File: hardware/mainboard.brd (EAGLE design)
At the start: 65 x 30 mm, 34 parts, among them IC1 ESP-12E/F, Q1 BC847BS, Q2 BC847BS, Q3 BC847BS

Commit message: Placing elements in layout
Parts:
- moved Q3 61.5 mm to (17.5, 14.5), flipped to the bottom
- moved C2 57.0 mm to (27.0, 2.50), flipped to the bottom
- moved C1 53.4 mm to (27.0, 5.50), flipped to the bottom
- moved R2 50.8 mm to (27.0, 11.5), flipped to the bottom, turned to 180 degrees
- moved R15 50.4 mm to (27.0, 14.5), flipped to the bottom
- moved R14 46.3 mm to (21.0, 5.50), flipped to the bottom
- moved R5 42.9 mm to (27.0, 8.50), flipped to the bottom, turned to 0 degrees
- moved Q2 42.0 mm to (17.5, 18.5), flipped to the bottom, turned to 270 degrees
- moved R22 36.5 mm to (35.5, 24.0), flipped to the bottom, turned to 180 degrees
- moved R10 32.8 mm to (29.5, 24.0), flipped to the bottom, turned to 180 degrees
- moved R13 23.9 mm to (35.5, 27.0), flipped to the bottom, turned to 180 degrees
- moved R9 20.6 mm to (29.5, 27.0), flipped to the bottom
- moved Q1 20.2 mm to (17.5, 22.5), flipped to the bottom, turned to 270 degrees
- moved R11 12.9 mm to (50.0, 26.0), flipped to the bottom, turned to 0 degrees
- moved R12 7.85 mm to (43.5, 26.0), flipped to the bottom, turned to 0 degrees
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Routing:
- net GND: track 9.57 -> 0.00 mm

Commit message: Layout resolved
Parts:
- moved R7 2.50 mm to (6.00, 12.0)
- moved R8 2.50 mm to (6.00, 14.5)
- moved R14 2.12 mm to (22.5, 7.00), turned to 270 degrees
- moved R11 1.41 mm to (49.0, 27.0)
- moved R12 1.12 mm to (43.0, 27.0)
- moved Q1 0.50 mm to (17.5, 22.0)
- moved Q2 0.25 mm to (17.5, 18.2)
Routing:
- net GND: track 0.00 -> 125.1 mm, vias 0 -> 5
- net +3V3: track 0.00 -> 87.8 mm, vias 0 -> 5
- net ESP12_/RESET: track 0.00 -> 59.5 mm, vias 0 -> 1
- net GPIO_RING_HOUSE_DETECT: track 0.00 -> 56.4 mm, vias 0 -> 2
- net ESP12_ENABLE: track 0.00 -> 37.9 mm, vias 0 -> 2
- net N$10: track 0.00 -> 33.4 mm
- net N$11: track 0.00 -> 33.3 mm
- net N$8: track 0.00 -> 25.1 mm, vias 0 -> 1
- net ESP12_/FWUPLOAD: track 4.15 -> 26.2 mm, vias 1 -> 2
- net N$9: track 0.00 -> 22.0 mm, vias 0 -> 2
- net N$3: track 0.00 -> 19.0 mm, vias 0 -> 1
- net GPIO_NO_RESET_ON_RING: track 0.00 -> 16.3 mm, vias 0 -> 1
- net RITTO_RING_HOUSE: track 0.00 -> 15.7 mm
- net N$1: track 0.00 -> 15.3 mm
- net GPIO_10_IN: track 3.70 -> 18.6 mm
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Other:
- outline, holes or cut-outs redrawn

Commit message: Checkpoint commit
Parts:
- turned RESET to 180 degrees
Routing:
- net GND: track 125.1 -> 128.1 mm, vias 5 -> 4
- net +3V3: track 87.8 -> 89.5 mm, vias 5 -> 3

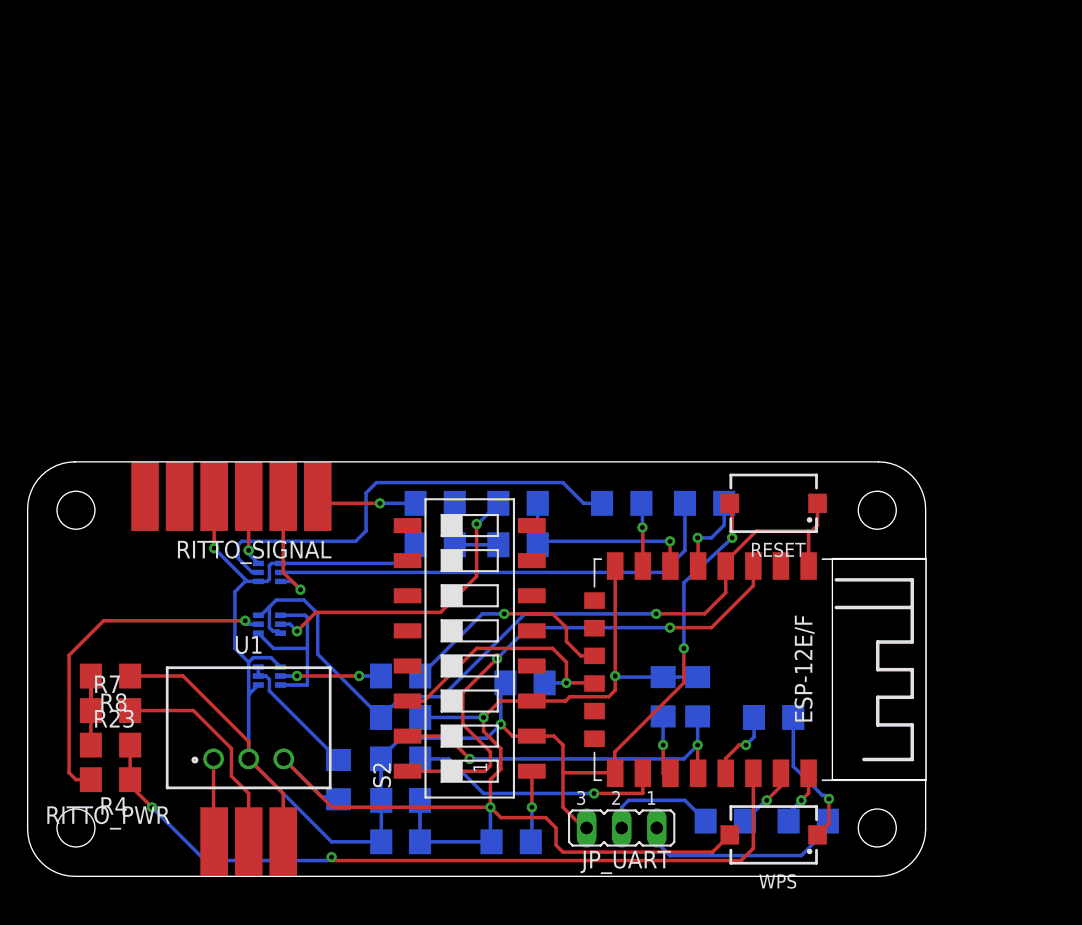
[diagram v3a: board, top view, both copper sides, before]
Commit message: Adding USB/FTDI
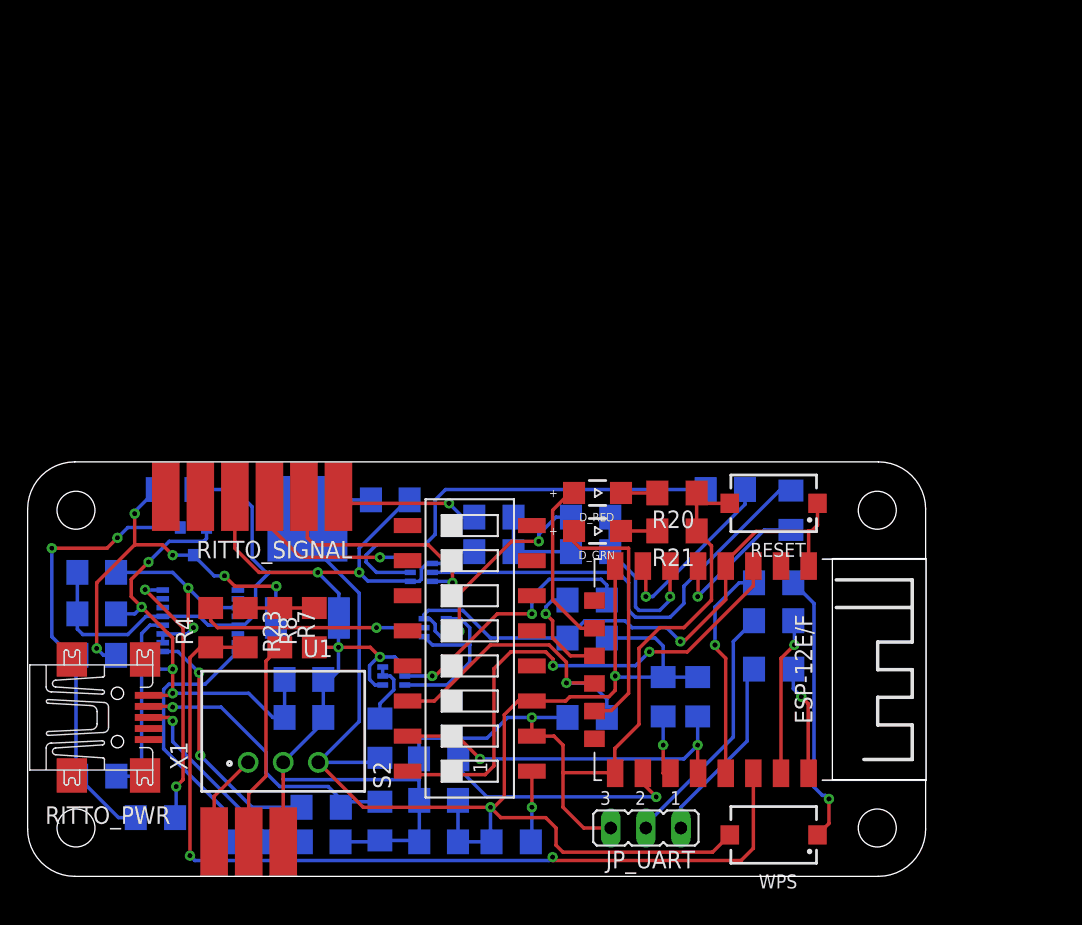
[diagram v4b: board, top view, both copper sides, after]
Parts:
- added C10, C9: 0.1uF, rcl:C1206
- added C11: 10uF, rcl:C1206
- added C3, C4: 47pF, rcl:C1206
- added C5: 4.7uF, rcl:C1206
- added C6, C8: 100nF, rcl:C1206
- added C7: 10nF, rcl:C1206
- added D_GRN, D_RED: (no value), 156120RS75300_Eagle_WL-SMRW_rev20b:WL-SMRW_1206_CYL
- added IC2: FT230XS, ftdichip:SSOP16
- added IC3: LD117ADT33TR, v-reg:DPACK
- added Q4: IRLML5203, transistor-power:MICRO3
- added R20, R21: 68, rcl:R1206
- added R24, R25: 27, rcl:R1206
- added R26, R27: 1k, rcl:R1206
- added X1: MINI-USB-UX60-MB-5ST, con-hirose:UX60-MB-5ST
- moved R8 15.2 mm to (20.8, 18.0), turned to 90 degrees
- moved R6 14.9 mm to (54.0, 18.5)
- moved R2 14.7 mm to (40.5, 17.2)
- moved R15 14.6 mm to (40.5, 20.0), turned to 180 degrees
- moved R7 13.6 mm to (18.2, 18.0), turned to 270 degrees
- moved R4 13.2 mm to (13.2, 18.0), turned to 90 degrees
- moved R23 12.9 mm to (15.8, 18.0), turned to 270 degrees
- moved Q2 12.0 mm to (29.5, 18.0)
- moved R3 11.3 mm to (54.0, 15.0), turned to 0 degrees
- moved Q1 11.0 mm to (28.5, 22.0)
- moved R1 9.75 mm to (54.0, 21.2)
- moved Q3 9.00 mm to (26.5, 14.5)
- moved R12 7.57 mm to (50.5, 28.0)
- moved R11 6.27 mm to (55.2, 26.5), turned to 90 degrees
- moved R13 5.34 mm to (40.8, 26.0)
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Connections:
- new net FTDI_VCCIO: C8.1, IC2.10, IC2.11, IC2.3
- new net LED_GRN: D_GRN.2, IC1.MOSI
- new net LED_RED: D_RED.2, IC1.MISO
- new net N$12: D_RED.1, R20.2
- new net N$13: D_GRN.1, R21.2
- new net N$17: IC2.9, R24.1
- new net N$18: C9.2, Q4.1, R26.1, R27.2
- new net N$19: IC2.8, R25.2
- new net N$20: C10.1, C9.1, IC3.3, Q4.3
- new net USB_CBUS3: IC2.16, R26.2
- new net USB_DM: C3.1, R24.2, X1.2
- new net USB_DP: C4.1, R25.1, X1.3
- new net USB_GND: X1.4
- new net USB_SHIELD: X1.5
- new net USB_VCC: C5.1, C6.1, C7.1, IC2.12, Q4.2, R27.1, X1.1
- net +3V3: now also C11.1, IC3.4
- net GND: now also C10.2, C11.2, C3.2, C4.2, C5.2, C6.2, C7.2, C8.2, IC2.13, IC2.5, IC3.1, R20.1, R21.1
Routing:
- net GND: track 128.1 -> 178.2 mm, vias 4 -> 5
- net USB_VCC: track 0.00 -> 48.2 mm, vias 0 -> 4
- net N$18: track 0.00 -> 33.0 mm, vias 0 -> 2
- net N$20: track 0.00 -> 28.7 mm, vias 0 -> 5
- net USB_DM: track 0.00 -> 21.2 mm, vias 0 -> 1
- net +3V3: track 89.5 -> 110.0 mm, vias 3 -> 2
- net N$19: track 0.00 -> 19.4 mm
- net USB_CBUS3: track 0.00 -> 19.2 mm, vias 0 -> 2
- net LED_GRN: track 0.00 -> 18.4 mm
- net N$17: track 0.00 -> 18.2 mm, vias 0 -> 2
- net ESP12_/RESET: track 59.8 -> 42.5 mm
- net USB_DP: track 0.00 -> 16.0 mm, vias 0 -> 1
- net FTDI_VCCIO: track 0.00 -> 15.9 mm, vias 0 -> 2
- net LED_RED: track 0.00 -> 12.4 mm
- net N$15: track 7.29 -> 19.5 mm
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
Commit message: Checkpoint commit layout
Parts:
- added R28, R29: 10k, rcl:R1206
- moved R24 9.30 mm to (13.8, 10.5)
- moved C10 4.96 mm to (14.0, 24.2)
- moved R12 4.70 mm to (46.2, 26.0)
- moved C9 3.81 mm to (3.50, 12.5), turned to 270 degrees
- moved R25 3.05 mm to (14.0, 5.00)
- moved C4 2.92 mm to (19.8, 5.00)
- moved IC3 2.75 mm to (20.2, 20.8)
- moved Q4 2.50 mm to (9.50, 24.2), turned to 0 degrees
- moved R5 2.25 mm to (29.8, 10.8)
- moved R3 1.75 mm to (54.0, 13.2)
- moved C1 1.50 mm to (29.8, 7.00)
- moved C6 1.46 mm to (20.8, 13.0)
- moved R11 1.35 mm to (54.0, 26.0), turned to 0 degrees
- moved C5 1.25 mm to (20.8, 10.5)
- moved R26 1.06 mm to (8.50, 5.00)
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- renumbered JP_UART to UART
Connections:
- new net N$21: IC2.4, R28.2
- new net N$22: IC2.6, R29.2
- net FTDI_VCCIO: now also R28.1, R29.1
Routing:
- net FTDI_VCCIO: track 15.9 -> 34.3 mm, vias 2 -> 3
- net N$22: track 0.00 -> 11.0 mm, vias 0 -> 2
- net N$21: track 0.00 -> 6.90 mm, vias 0 -> 1
- net GND: track 178.2 -> 173.6 mm
- net UART_RX: track 11.5 -> 15.5 mm
- net GPIO_MUTE: track 13.3 -> 9.55 mm
- net N$11: track 32.0 -> 28.4 mm
- net USB_CBUS3: track 19.2 -> 22.7 mm
- net N$10: track 33.0 -> 29.7 mm
- net +3V3: track 110.0 -> 107.0 mm
- net N$20: track 28.7 -> 31.5 mm, vias 5 -> 4
- net USB_DP: track 16.0 -> 13.3 mm
- net N$17: track 18.2 -> 16.1 mm
- net N$19: track 19.4 -> 17.4 mm
- net GPIO_NO_RESET_ON_RING: track 7.81 -> 9.68 mm
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
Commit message: Finalizing board file
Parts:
- added 3V3, GND, HSE: TPTP10SQ, testpad:TP10SQ
- moved R23 0.56 mm to (16.2, 17.8)
- moved R4 0.56 mm to (13.8, 17.8)
- moved R7 0.56 mm to (18.8, 17.8)
- moved R8 0.56 mm to (21.2, 17.8)
- moved IC2 0.50 mm to (12.0, 18.5)
- renumbered RITTO_PWR to PWR, RITTO_SIGNAL to SIGNAL
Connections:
- removed net USB_GND: X1.4
- net +3V3: now also 3V3.TP
- net GND: now also GND.TP, X1.4
- net RITTO_RING_HOUSE: now also HSE.TP
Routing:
- net GND: track 173.6 -> 195.3 mm, vias 5 -> 7
- net RITTO_RING_HOUSE: track 15.0 -> 26.8 mm
- net USB_CBUS3: track 22.7 -> 18.1 mm
- net +3V3: track 107.0 -> 111.3 mm
- net N$22: track 11.0 -> 12.5 mm
- net N$17: track 16.1 -> 17.2 mm
- net N$19: track 17.4 -> 18.3 mm
- net FTDI_VCCIO: track 34.3 -> 34.9 mm
- net N$21: track 6.90 -> 6.40 mm
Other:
- board text added: "+24V"
- board text added: "ENABLE"
- board text added: "FLASH"
- board text added: "GND"
- board text added: "GPIO10"
- board text added: "HOME"
- board text added: "HOUSE"
- board text added: "MUTE"
- board text added: "OPEN"
- board text added: "RX"
- board text added: "TX"
- board text added: "VCC"
- board text added: "WIFI_RING v1.0 KKR 24/2020"
